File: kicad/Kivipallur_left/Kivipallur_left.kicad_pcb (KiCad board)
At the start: 2 copper layers, 156.2 x 103.9 mm, 29 parts, among them J1 TRRS, SW1 SW_Push, SW10 SW_Push, SW11 SW_Push, SW12 SW_Push, SW13 SW_Push, SW14 SW_Push, SW15 SW_Push, SW16 SW_Push, SW17 SW_Push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

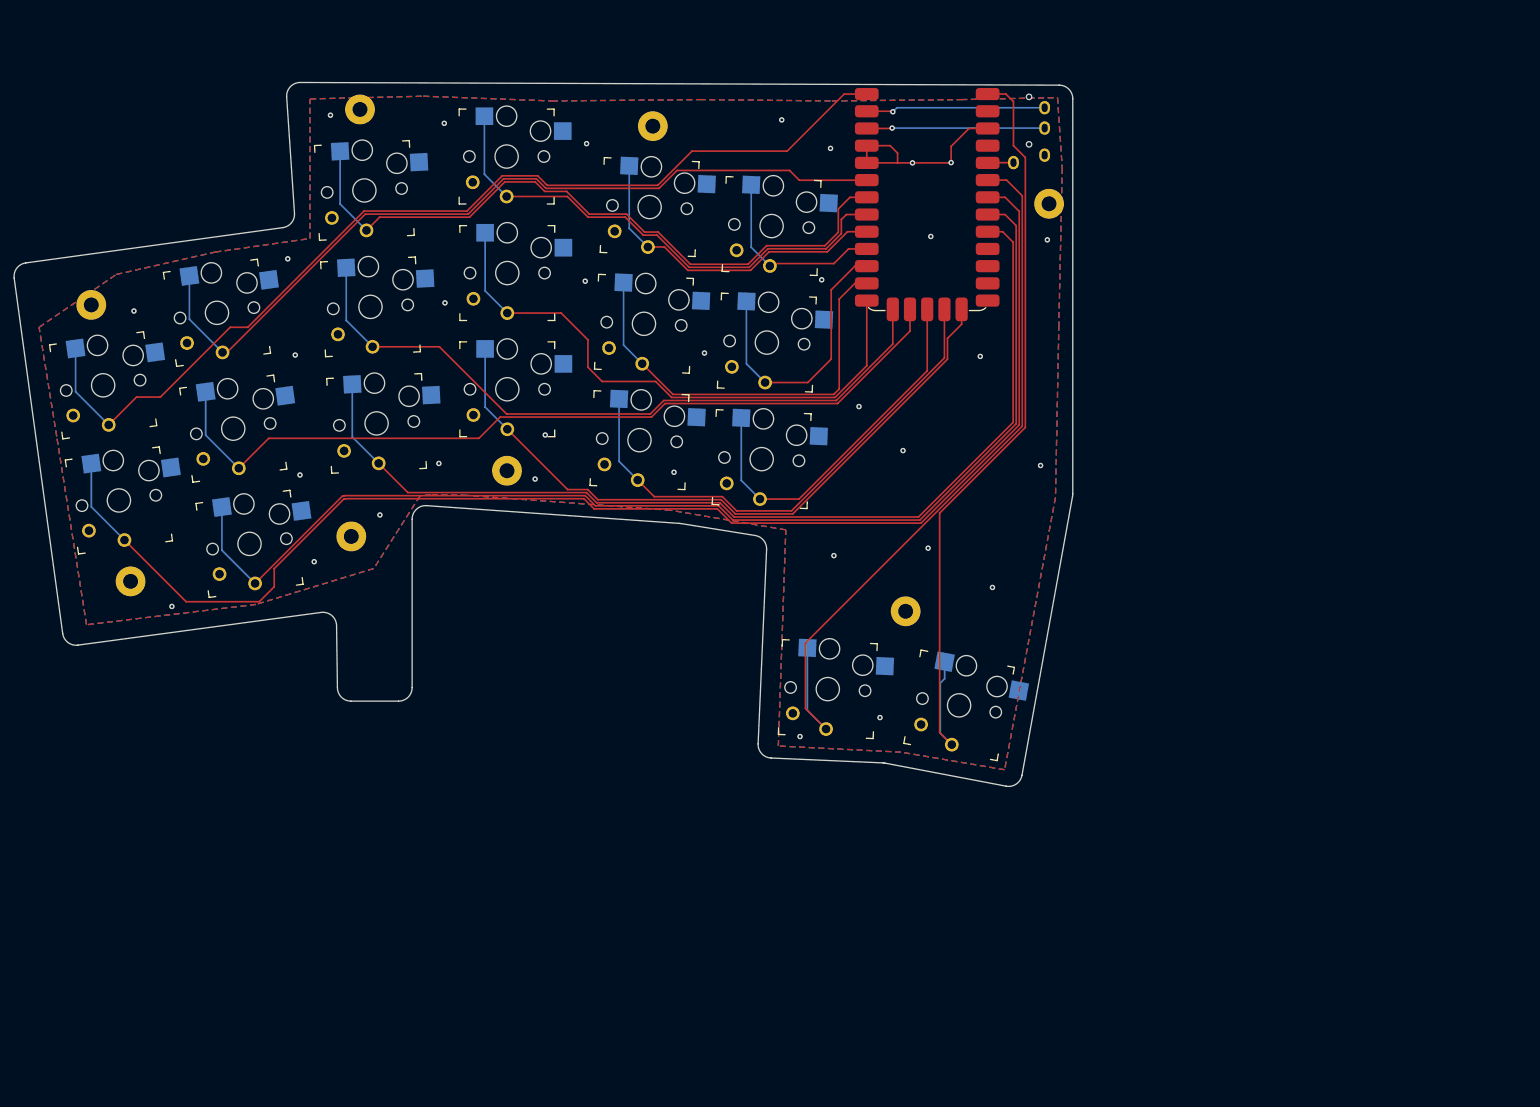
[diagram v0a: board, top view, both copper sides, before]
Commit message: Add final ergogen config
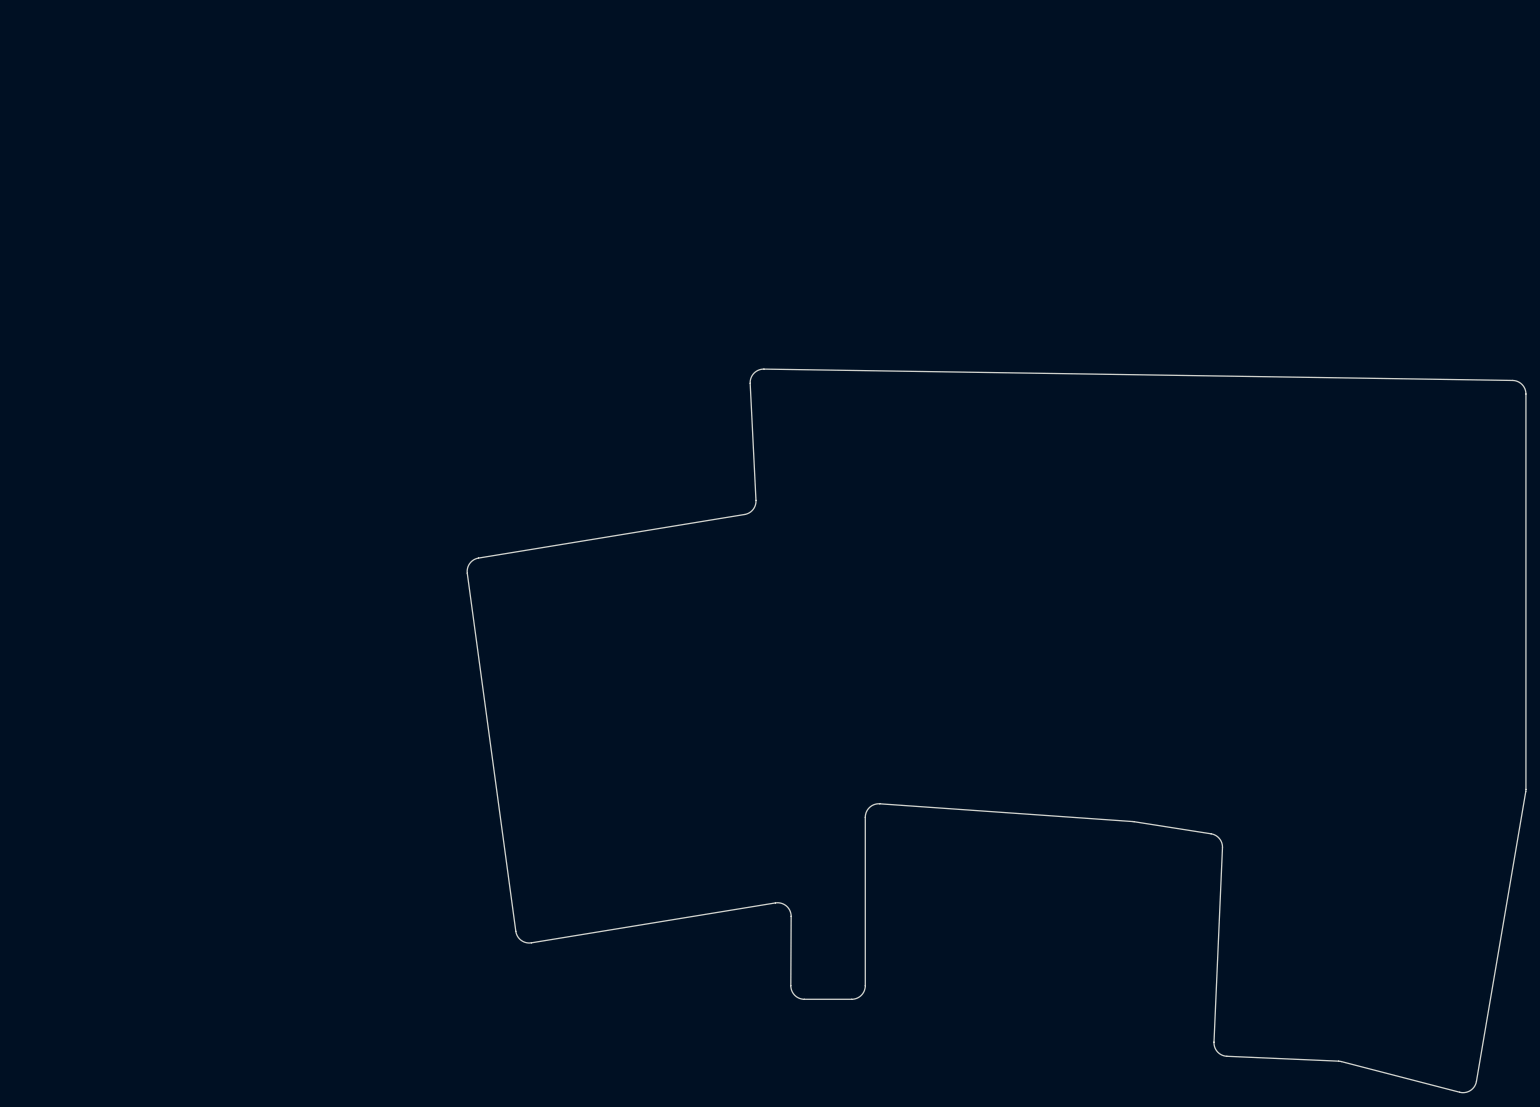
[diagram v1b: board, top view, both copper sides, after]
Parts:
- removed H1, H2, H3, H4, H5, H6, H7, H8: MountingHole, MountingHole:MountingHole_2.2mm_M2_Pad
- removed J1: TRRS, Keebio-Parts:TRRS-PJ-320A
- removed SW1, SW10, SW11, SW12, SW13, SW14, SW15, SW16, SW17, SW18, SW19, SW2, SW3, SW4, SW5, SW6, SW7, SW8, SW9: SW_Push, keyswitches:Kailh_socket_PG1350_optional
- removed U1: Helios, PCM_marbastlib-xp-promicroish:Helios_AC
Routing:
- net /OUTER_BOTTOM: track 201.5 -> 0.00 mm
- net /PINKY_BOTTOM: track 172.5 -> 0.00 mm
- net /RING_BOTTOM: track 147.0 -> 0.00 mm
- net /OUTER_TOP: track 146.6 -> 0.00 mm
- net /PINKY_HOME: track 124.0 -> 0.00 mm
- net /PINKY_TOP: track 121.3 -> 0.00 mm
- net /THUMB_RIGHT: track 119.1 -> 0.00 mm
- net /THUMB_LEFT: track 112.4 -> 0.00 mm
- net /RING_HOME: track 103.5 -> 0.00 mm
- net /RING_TOP: track 101.2 -> 0.00 mm
- net /MIDDLE_BOTTOM: track 101.0 -> 0.00 mm
- net /MIDDLE_HOME: track 85.3 -> 0.00 mm
- net /INDEX_BOTTOM: track 76.8 -> 0.00 mm
- net /MIDDLE_TOP: track 75.1 -> 0.00 mm
- net /INDEX_HOME: track 62.7 -> 0.00 mm
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- removed copper zone on B.Cu, net GND
- removed copper zone on F.Cu, net GND
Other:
- board size 156.2 x 103.9 mm -> 156.3 x 106.8 mm
- rule pad_to_mask_clearance: 0 -> 0.05

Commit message: Add left hand PCB
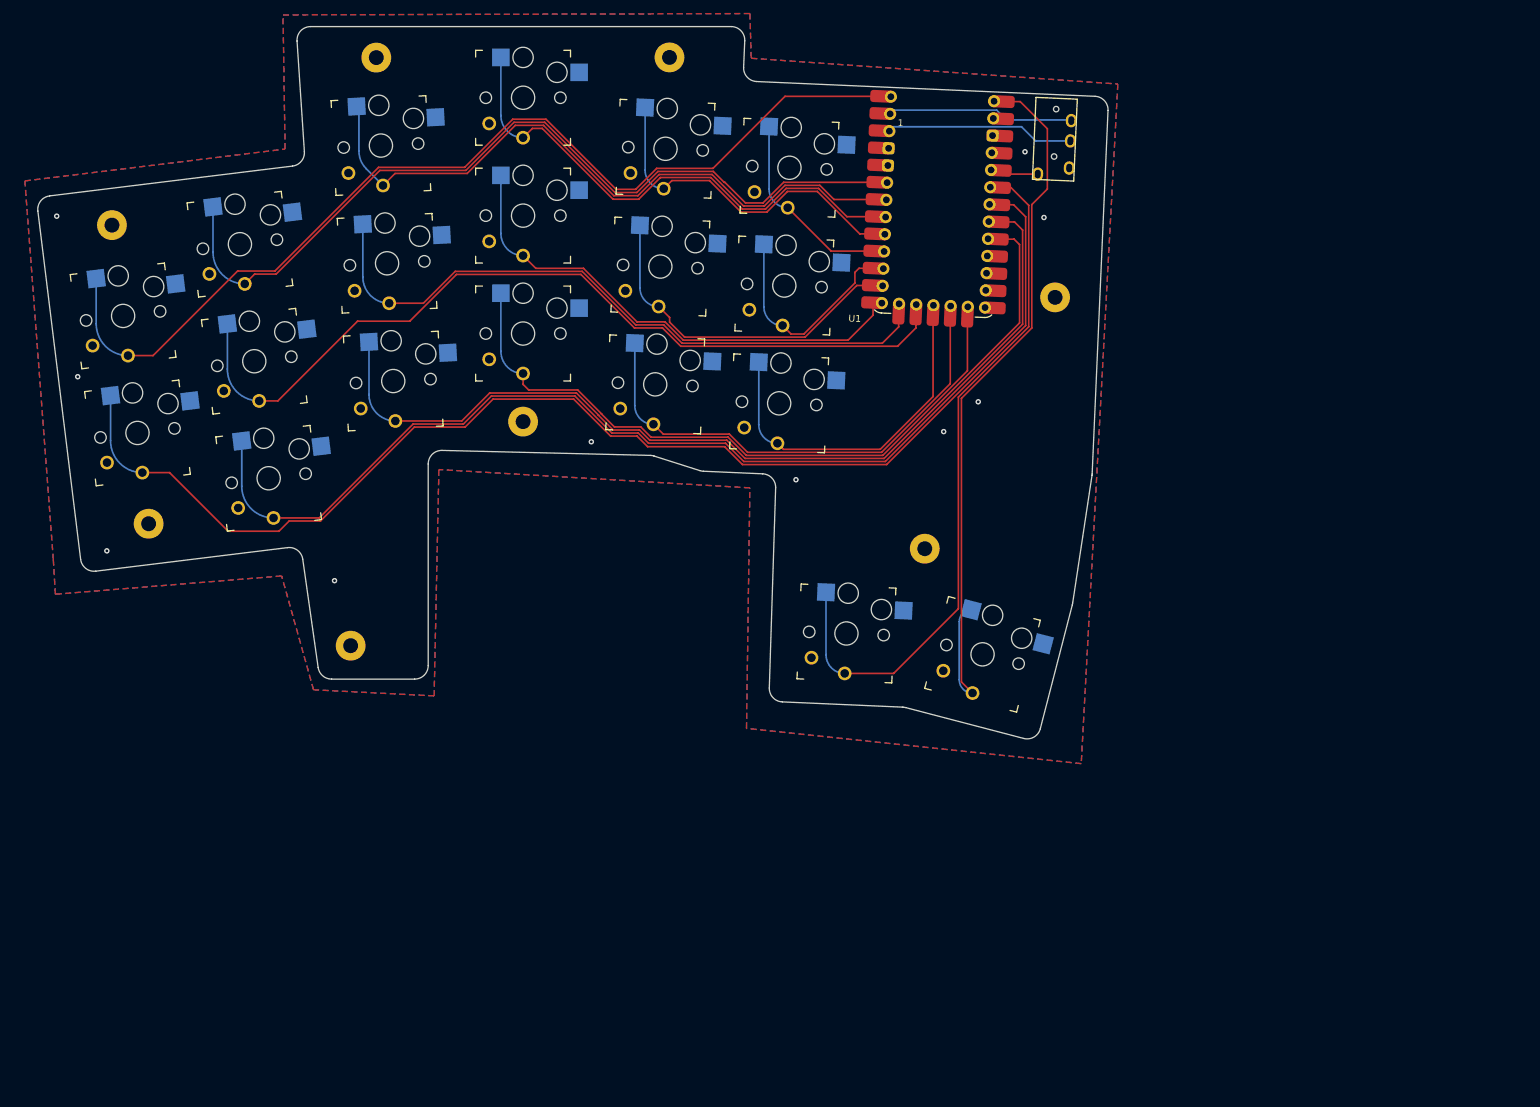
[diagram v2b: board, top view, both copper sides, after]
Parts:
- added H1: MountingHole, MountingHole:MountingHole_2.2mm_M2_Pad, F.Cu at (69.8, 67.0)
- added H2: MountingHole, MountingHole:MountingHole_2.2mm_M2_Pad, F.Cu at (75.2, 111.1)
- added H3: MountingHole, MountingHole:MountingHole_2.2mm_M2_Pad, F.Cu at (105.0, 129.1)
- added H4: MountingHole, MountingHole:MountingHole_2.2mm_M2_Pad, F.Cu at (130.4, 96.0)
- added H5: MountingHole, MountingHole:MountingHole_2.2mm_M2_Pad, F.Cu at (108.8, 42.3)
- added H6: MountingHole, MountingHole:MountingHole_2.2mm_M2_Pad, F.Cu at (152.0, 42.3)
- added H7: MountingHole, MountingHole:MountingHole_2.2mm_M2_Pad, F.Cu at (208.9, 77.7)
- added H8: MountingHole, MountingHole:MountingHole_2.2mm_M2_Pad, F.Cu at (189.7, 114.8)
- added J1: TRRS, Keebio-Parts:TRRS-PJ-320A, F.Cu at (209.2, 48.3)
- added SW1: SW_Push, keyswitches:Kailh_socket_PG1350_optional, F.Cu at (71.4, 80.4)
- added SW10: SW_Push, keyswitches:Kailh_socket_PG1350_optional, F.Cu at (130.4, 65.6)
- added SW11: SW_Push, keyswitches:Kailh_socket_PG1350_optional, F.Cu at (130.4, 83.0)
- added SW12: SW_Push, keyswitches:Kailh_socket_PG1350_optional, F.Cu at (151.4, 55.8)
- added SW13: SW_Push, keyswitches:Kailh_socket_PG1350_optional, F.Cu at (150.7, 73.1)
- added SW14: SW_Push, keyswitches:Kailh_socket_PG1350_optional, F.Cu at (149.9, 90.5)
- added SW15: SW_Push, keyswitches:Kailh_socket_PG1350_optional, F.Cu at (169.7, 58.6)
- added SW16: SW_Push, keyswitches:Kailh_socket_PG1350_optional, F.Cu at (169.0, 75.9)
- added SW17: SW_Push, keyswitches:Kailh_socket_PG1350_optional, F.Cu at (168.2, 93.3)
- added SW18: SW_Push, keyswitches:Kailh_socket_PG1350_optional, F.Cu at (178.2, 127.3)
- added SW19: SW_Push, keyswitches:Kailh_socket_PG1350_optional, F.Cu at (198.2, 130.4)
- added SW2: SW_Push, keyswitches:Kailh_socket_PG1350_optional, F.Cu at (73.5, 97.7)
- added SW3: SW_Push, keyswitches:Kailh_socket_PG1350_optional, F.Cu at (88.6, 69.8)
- added SW4: SW_Push, keyswitches:Kailh_socket_PG1350_optional, F.Cu at (90.8, 87.1)
- added SW5: SW_Push, keyswitches:Kailh_socket_PG1350_optional, F.Cu at (92.9, 104.4)
- added SW6: SW_Push, keyswitches:Kailh_socket_PG1350_optional, F.Cu at (109.4, 55.3)
- added SW7: SW_Push, keyswitches:Kailh_socket_PG1350_optional, F.Cu at (110.4, 72.7)
- added SW8: SW_Push, keyswitches:Kailh_socket_PG1350_optional, F.Cu at (111.3, 90.0)
- added SW9: SW_Push, keyswitches:Kailh_socket_PG1350_optional, F.Cu at (130.4, 48.2)
- added U1: Helios, PCM_marbastlib-xp-promicroish:Helios_ACH, F.Cu at (191.6, 64.9)
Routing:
- net /OUTER_BOTTOM: track 0.00 -> 189.2 mm
- net /PINKY_BOTTOM: track 0.00 -> 162.3 mm
- net /OUTER_TOP: track 0.00 -> 149.6 mm
- net /RING_BOTTOM: track 0.00 -> 135.1 mm
- net /PINKY_HOME: track 0.00 -> 126.2 mm
- net /PINKY_TOP: track 0.00 -> 126.0 mm
- net /THUMB_RIGHT: track 0.00 -> 111.7 mm
- net /THUMB_LEFT: track 0.00 -> 103.5 mm
- net /RING_TOP: track 0.00 -> 99.4 mm
- net /MIDDLE_BOTTOM: track 0.00 -> 98.5 mm
- net /RING_HOME: track 0.00 -> 98.4 mm
- net /MIDDLE_TOP: track 0.00 -> 76.9 mm
- net /MIDDLE_HOME: track 0.00 -> 73.8 mm
- net /INDEX_BOTTOM: track 0.00 -> 73.3 mm
- net /INNER_BOTTOM: track 0.00 -> 52.2 mm
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- added copper zone on B.Cu, net GND
- added copper zone on F.Cu, net GND
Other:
- board size 156.3 x 106.8 mm -> 158 x 105.1 mm

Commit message: Change PMW3360 footprint outline, finalize others
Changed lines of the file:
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@@
 			(plot_on_all_layers_selection 0x0000000_00000000)
 			(disableapertmacros no)
-			(usegerberextensions no)
-			(usegerberattributes yes)
-			(usegerberadvancedattributes yes)
-			(creategerberjobfile yes)
+			(usegerberextensions yes)
+			(usegerberattributes no)
+			(usegerberadvancedattributes no)
+			(creategerberjobfile no)
 			(dashed_line_dash_ratio 12.000000)
 			(dashed_line_gap_ratio 3.000000)
@@
 			(psa4output no)
 			(plotreference yes)
-			(plotvalue yes)
+			(plotvalue no)
 			(plotfptext yes)
 			(plotinvisibletext no)
 			(sketchpadsonfab no)
-			(subtractmaskfromsilk no)
+			(subtractmaskfromsilk yes)
 			(outputformat 1)
 			(mirror no)
-			(drillshape 1)
+			(drillshape 0)
 			(scaleselection 1)
-			(outputdirectory "")
+			(outputdirectory "../../gerbers/Kivipallur_left/")
 		)
 	)
@@
 		(fp_line
 			(start 7 -6.2)
-			(end 2.5 -6.200003)
+			(end 2.5 -6.200004)
 			(stroke
 				(width 0.15)
@@
 		)
 		(fp_arc
-			(start 2.5 -6.200003)
-			(mid 2.146448 -6.346448)
+			(start 2.5 -6.200004)
+			(mid 2.146449 -6.346449)
 			(end 2 -6.7)
 			(stroke
@@
 		(fp_line
 			(start 7 -6.2)
-			(end 2.5 -6.200003)
+			(end 2.5 -6.200004)
 			(stroke
 				(width 0.15)
@@
 		)
 		(fp_arc
-			(start 2.5 -6.200003)
-			(mid 2.146448 -6.346448)
+			(start 2.5 -6.200004)
+			(mid 2.146449 -6.346449)
 			(end 2 -6.7)
 			(stroke
@@
 		(fp_line
 			(start 7 -6.2)
-			(end 2.5 -6.200003)
+			(end 2.5 -6.200004)
 			(stroke
 				(width 0.15)
@@
 		)
 		(fp_arc
-			(start 2.5 -6.200003)
-			(mid 2.146448 -6.346448)
+			(start 2.5 -6.200004)
+			(mid 2.146449 -6.346449)
 			(end 2 -6.7)
 			(stroke
@@
 		(fp_line
 			(start 7 -6.2)
-			(end 2.5 -6.200003)
+			(end 2.5 -6.200004)
 			(stroke
 				(width 0.15)
@@
 		)
 		(fp_arc
-			(start 2.5 -6.200003)
-			(mid 2.146448 -6.346448)
+			(start 2.5 -6.200004)
+			(mid 2.146449 -6.346449)
 			(end 2 -6.7)
 			(stroke
@@
 		(fp_line
 			(start 7 -6.2)
-			(end 2.5 -6.200003)
+			(end 2.5 -6.200004)
 			(stroke
 				(width 0.15)
@@
 		)
 		(fp_arc
-			(start 2.5 -6.200003)
-			(mid 2.146448 -6.346448)
+			(start 2.5 -6.200004)
+			(mid 2.146449 -6.346449)
 			(end 2 -6.7)
 			(stroke
@@
 		(fp_line
 			(start 7 -6.2)
-			(end 2.5 -6.200003)
+			(end 2.5 -6.200004)
 			(stroke
 				(width 0.15)
@@
 		)
 		(fp_arc
-			(start 2.5 -6.200003)
-			(mid 2.146448 -6.346448)
+			(start 2.5 -6.200004)
+			(mid 2.146449 -6.346449)
 			(end 2 -6.7)
 			(stroke
@@
 		)
 		(fp_line
-			(start -6.999997 -6)
+			(start -6.999996 -6)
 			(end -7 -7)
 			(stroke
@@
 		(fp_line
 			(start -7 7)
-			(end -6 6.999997)
+			(end -6 6.999996)
 			(stroke
 				(width 0.15)
@@
 		(fp_line
 			(start 7 -7)
-			(end 6 -6.999997)
+			(end 6 -6.999996)
 			(stroke
 				(width 0.15)
@@
 		)
 		(fp_line
-			(start 6.999997 6)
+			(start 6.999996 6)
 			(end 7 7)
 			(stroke
@@
 		(fp_line
 			(start 7 -6.2)
-			(end 2.5 -6.200003)
+			(end 2.5 -6.200004)
 			(stroke
 				(width 0.15)
@@
 		)
 		(fp_arc
-			(start 2.5 -6.200003)
-			(mid 2.146448 -6.346448)
+			(start 2.5 -6.200004)
+			(mid 2.146449 -6.346449)
 			(end 2 -6.7)
 			(stroke
@@
 		(fp_line
 			(start 7 -6.2)
-			(end 2.5 -6.200003)
+			(end 2.5 -6.200004)
 			(stroke
 				(width 0.15)
@@
 		)
 		(fp_arc
-			(start 2.5 -6.200003)
-			(mid 2.146448 -6.346448)
+			(start 2.5 -6.200004)
+			(mid 2.146449 -6.346449)
 			(end 2 -6.7)
 			(stroke
@@
 		(fp_line
 			(start 7 -6.2)
-			(end 2.5 -6.200003)
+			(end 2.5 -6.200004)
 			(stroke
 				(width 0.15)
@@
 		)
 		(fp_arc
-			(start 2.5 -6.200003)
-			(mid 2.146448 -6.346448)
+			(start 2.5 -6.200004)
+			(mid 2.146449 -6.346449)
 			(end 2 -6.7)
 			(stroke
@@
 		(fp_line
 			(start 7 -6.2)
-			(end 2.5 -6.200003)
+			(end 2.5 -6.200004)
 			(stroke
 				(width 0.15)
@@
 		)
 		(fp_arc
-			(start 2.5 -6.200003)
-			(mid 2.146448 -6.346448)
+			(start 2.5 -6.200004)
+			(mid 2.146449 -6.346449)
 			(end 2 -6.7)
 			(stroke
@@
 		)
 		(fp_line
-			(start -6.999997 -6)
+			(start -6.999996 -6)
 			(end -7 -7)
 			(stroke
@@
 		(fp_line
 			(start -7 7)
-			(end -6 6.999997)
+			(end -6 6.999996)
 			(stroke
 				(width 0.15)
@@
 		(fp_line
 			(start 7 -7)
-			(end 6 -6.999997)
+			(end 6 -6.999996)
 			(stroke
 				(width 0.15)
@@
 		)
 		(fp_line
-			(start 6.999997 6)
+			(start 6.999996 6)
 			(end 7 7)
 			(stroke
@@
 			(at -10.58 16.44 177.5)
 			(layer "F.SilkS")
+			(hide yes)
 			(effects
 				(font
@@
 		(fp_arc
 			(start -7.62 15.44)
-			(mid -8.182545 15.328104)
+			(mid -8.182545 15.328105)
 			(end -8.659447 15.009447)
 			(stroke
@@
 		(fp_line
 			(start 7 -6.2)
-			(end 2.5 -6.200003)
+			(end 2.5 -6.200004)
 			(stroke
 				(width 0.15)
@@
 		)
 		(fp_arc
-			(start 2.5 -6.200003)
-			(mid 2.146448 -6.346448)
+			(start 2.5 -6.200004)
+			(mid 2.146449 -6.346449)
 			(end 2 -6.7)
 			(stroke
@@
 		(fp_line
 			(start 7 -6.2)
-			(end 2.5 -6.200003)
+			(end 2.5 -6.200004)
 			(stroke
 				(width 0.15)
@@
 		)
 		(fp_arc
-			(start 2.5 -6.200003)
-			(mid 2.146448 -6.346448)
+			(start 2.5 -6.200004)
+			(mid 2.146449 -6.346449)
 			(end 2 -6.7)
 			(stroke
@@
 		)
 		(fp_line
-			(start -6.999997 -6)
+			(start -6.999996 -6)
 			(end -7 -7)
 			(stroke
@@
 		(fp_line
 			(start -7 7)
-			(end -6 6.999997)
+			(end -6 6.999996)
 			(stroke
 				(width 0.15)
@@
 		(fp_line
 			(start 7 -7)
-			(end 6 -6.999997)
+			(end 6 -6.999996)
 			(stroke
 				(width 0.15)
@@
 		)
 		(fp_line
-			(start 6.999997 6)
+			(start 6.999996 6)
 			(end 7 7)
 			(stroke
@@
 		(fp_line
 			(start 7 -6.2)
-			(end 2.5 -6.200003)
+			(end 2.5 -6.200004)
 			(stroke
 				(width 0.15)
@@
 		)
 		(fp_arc
-			(start 2.5 -6.200003)
-			(mid 2.146448 -6.346448)
+			(start 2.5 -6.200004)
+			(mid 2.146449 -6.346449)
 			(end 2 -6.7)
 			(stroke
@@
 		(fp_line
 			(start 7 -6.2)
-			(end 2.5 -6.200003)
+			(end 2.5 -6.200004)
 			(stroke
 				(width 0.15)
@@
 		)
 		(fp_arc
-			(start 2.5 -6.200003)
-			(mid 2.146448 -6.346448)
+			(start 2.5 -6.200004)
+			(mid 2.146449 -6.346449)
 			(end 2 -6.7)
 			(stroke
